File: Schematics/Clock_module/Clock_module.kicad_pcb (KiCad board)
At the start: 2 copper layers, 101.6 x 78.7 mm, 44 parts, among them J1 Conn_01x06_Female, J2 Power Input, SW1 Mode, SW2 Step, U1 NE555, U2 NE555, U3 NE555, U4 74LS04, U5 74LS32, U6 74LS08

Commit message: PCB RC1
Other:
- board text added: "Clock module"
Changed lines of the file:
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@@
-(kicad_pcb (version 20171130) (host pcbnew "(5.1.5-0-10_14)")
+(kicad_pcb (version 20171130) (host pcbnew "(5.1.5)-3")
   (general
     (thickness 1.6)
-    (drawings 26)
+    (drawings 27)
     (tracks 231)
     (zones 0)
@@
     (solder_mask_min_width 0.25)
     (aux_axis_origin 0 0)
-    (visible_elements FFFFFF7F)
+    (visible_elements 7FFFFFFF)
     (pcbplotparams
-      (layerselection 0x010fc_ffffffff)
-      (usegerberextensions false)
+      (layerselection 0x010f0_ffffffff)
+      (usegerberextensions true)
       (usegerberattributes false)
       (usegerberadvancedattributes false)
@@
       (psa4output false)
       (plotreference true)
-      (plotvalue true)
+      (plotvalue false)
       (plotinvisibletext false)
       (padsonsilk false)
@@
       (outputformat 1)
       (mirror false)
-      (drillshape 1)
+      (drillshape 0)
       (scaleselection 1)
-      (outputdirectory ""))
+      (outputdirectory "Gerber/"))
   )
   (net 0 "")
@@
     )
   )
-  (gr_text "Board revision: v001" (at 223.52 99.06) (layer F.SilkS)
+  (gr_text "Author: Dawid Buchwald" (at 223.52 95.25) (layer F.SilkS)
+    (effects (font (size 1.7 1.7) (thickness 0.2)) (justify left))
+  )
+  (gr_text "Board revision: v001" (at 223.52 101.092) (layer F.SilkS)
     (effects (font (size 1 1) (thickness 0.15)) (justify left))
   )
-  (gr_text https://github.com/dbuchwald/6502 (at 223.52 97.282) (layer F.SilkS)
+  (gr_text https://github.com/dbuchwald/6502 (at 223.52 99.314) (layer F.SilkS)
     (effects (font (size 1 1) (thickness 0.15)) (justify left))
   )
-  (gr_text "Based on Ben Eater’s design" (at 223.52 95.504) (layer F.SilkS)
+  (gr_text "Based on Ben Eater’s design" (at 223.52 97.536) (layer F.SilkS)
     (effects (font (size 1 1) (thickness 0.15)) (justify left))
   )
-  (gr_text "Author: Dawid Buchwald" (at 223.52 92.456) (layer F.SilkS)
+  (gr_text "Clock module" (at 223.52 92.456) (layer F.SilkS)
     (effects (font (size 2 2) (thickness 0.2)) (justify left))
   )

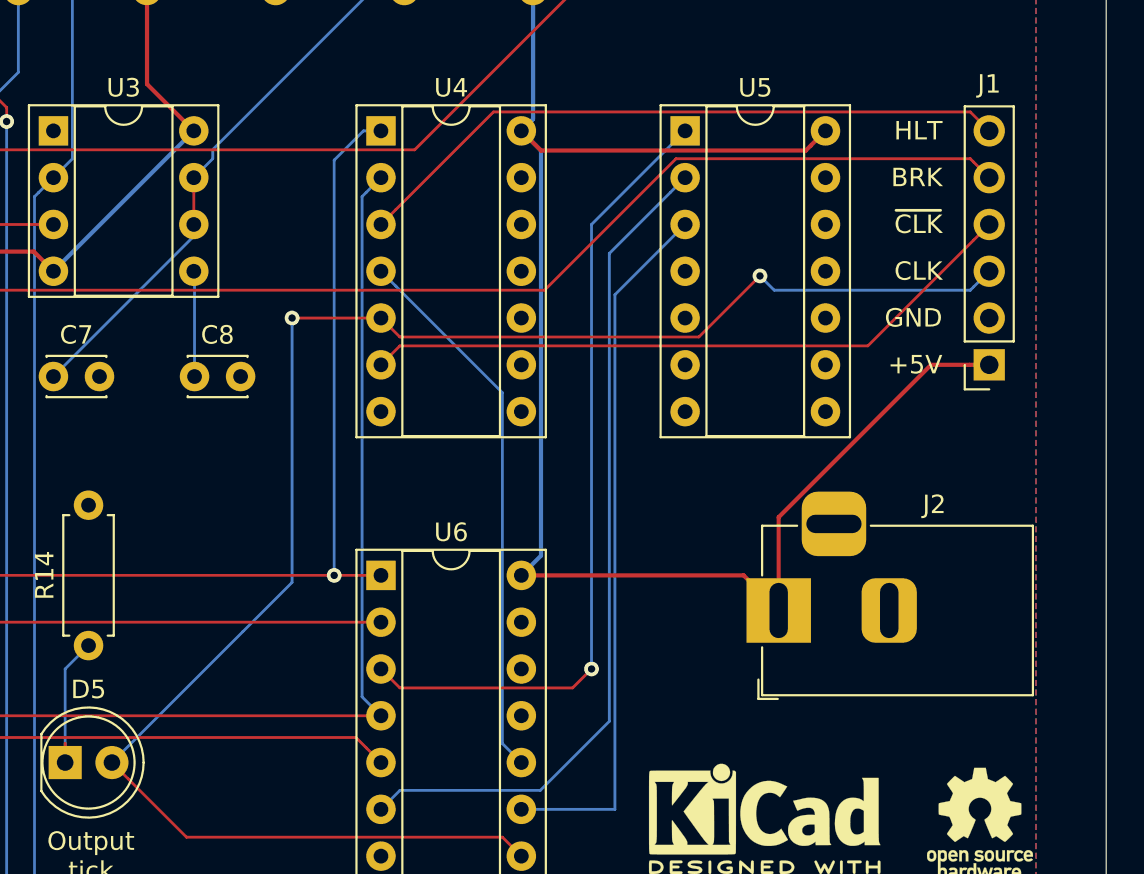
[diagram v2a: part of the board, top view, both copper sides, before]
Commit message: Added missing pull-down resistor to clock module
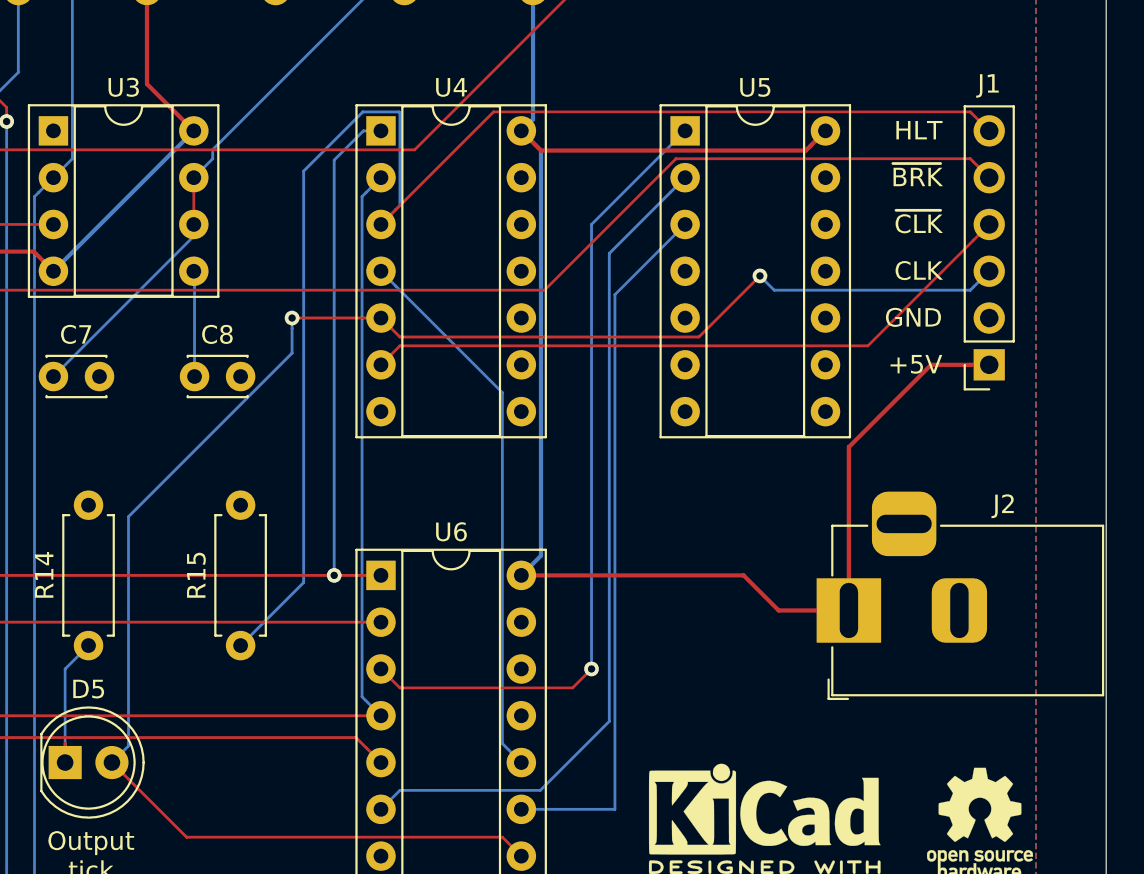
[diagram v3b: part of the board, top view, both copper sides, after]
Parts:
- added R15: 1K, Resistor_THT:R_Axial_DIN0207_L6.3mm_D2.5mm_P7.62mm_Horizontal, F.Cu at (221.0, 76.2)
- moved J2 3.81 mm to (254.0, 74.3)
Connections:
- net BRK renamed ~BRK
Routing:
- net HLT: track 36.0 -> 76.2 mm
- net VCC: track 208.9 -> 211.1 mm
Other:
- board text added: "~BRK"
- board text removed: "BRK"
